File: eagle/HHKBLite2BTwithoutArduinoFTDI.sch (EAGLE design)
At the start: 47 parts, among them CON1 45045-1445, CON2 45045-0845, IC1 4514N, IC2 4512N, IC4 HT7750A

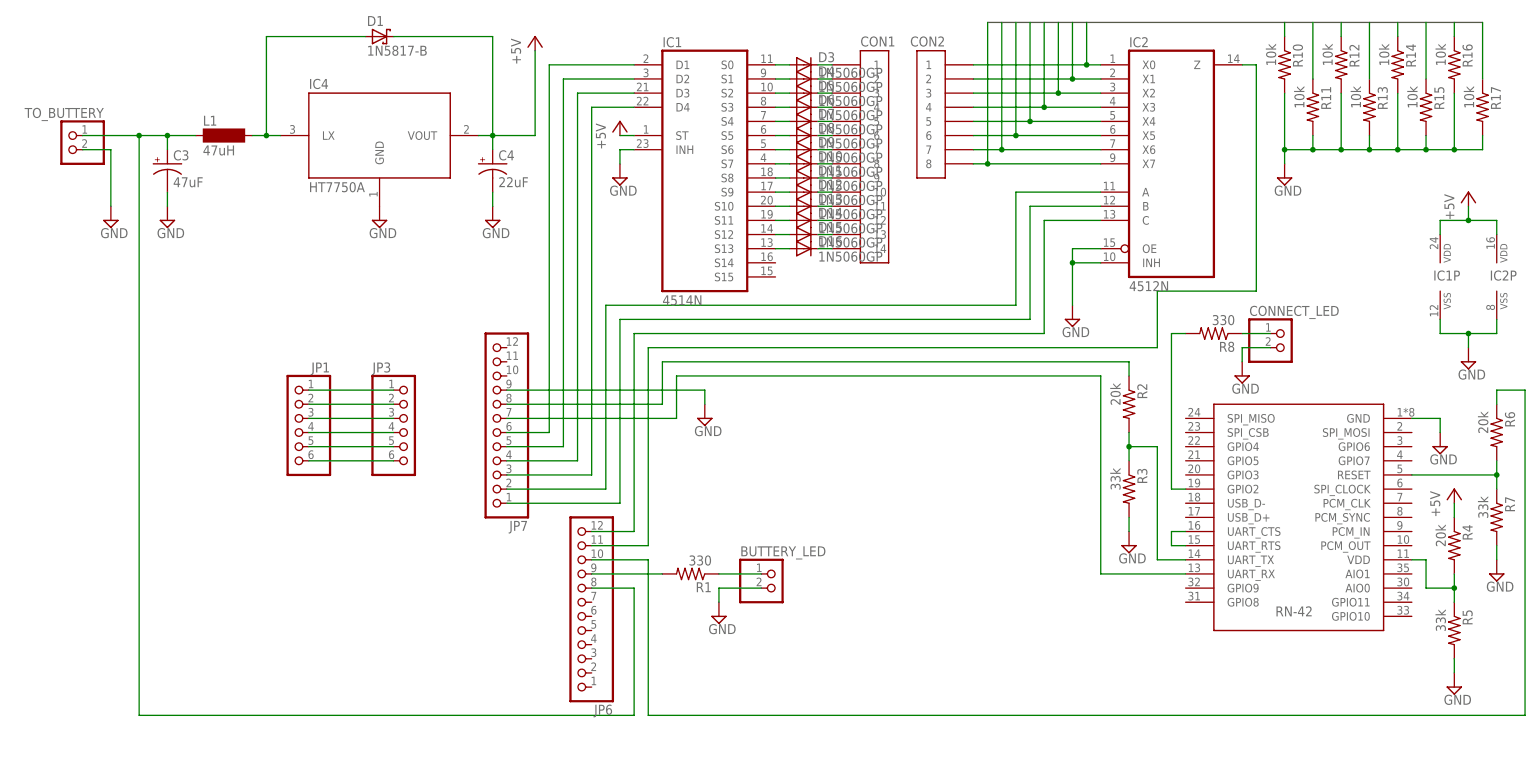
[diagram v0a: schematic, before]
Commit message: 基板を作成。
これまでは Arduino のpin1からpinNまでを順番につないでいたが、
基板に起こしやすいよう、接続の順番を基板用に書き換えた。
加えて、基板を作成した。
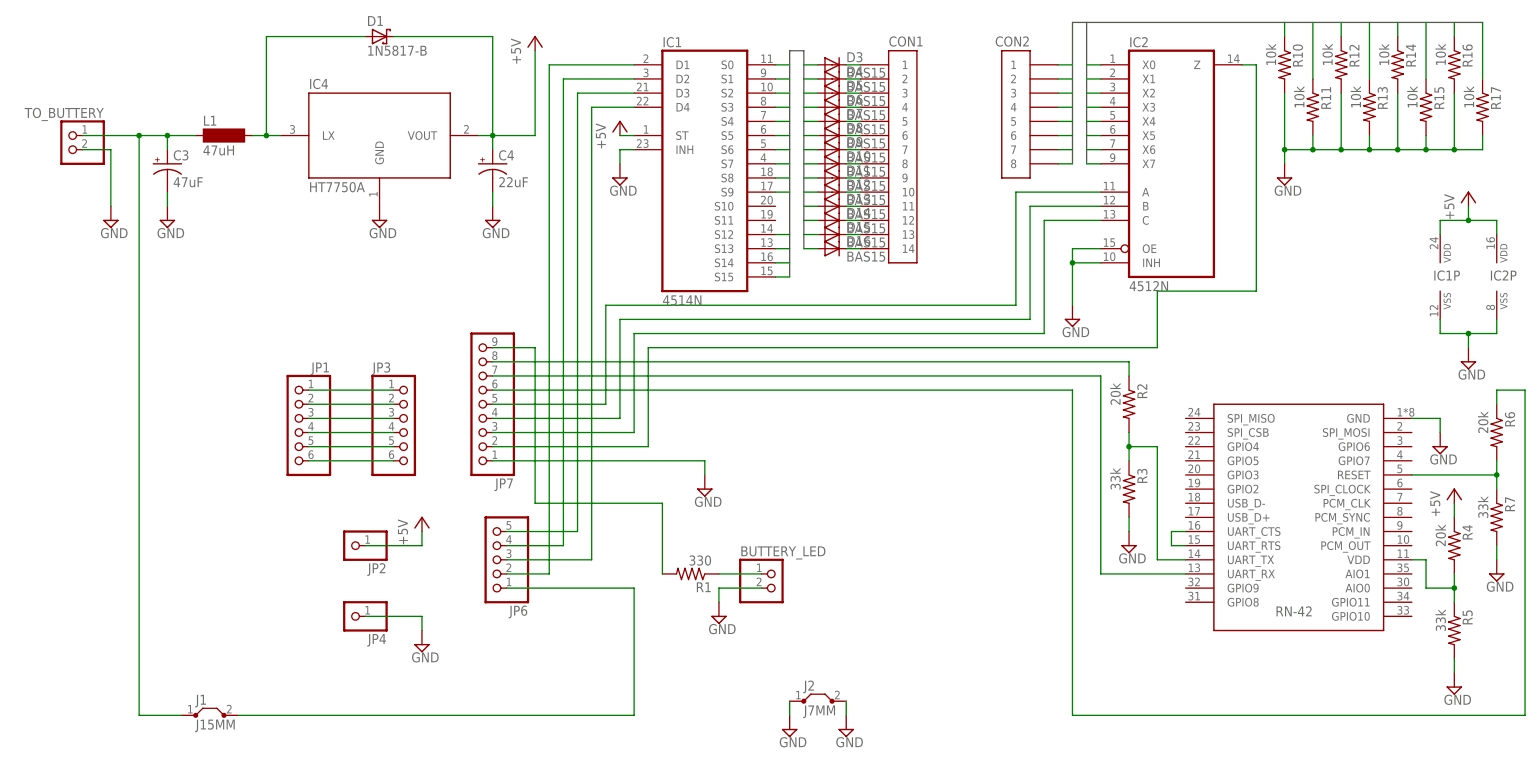
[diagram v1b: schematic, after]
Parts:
- removed CONNECT_LED: (no value), pinhead:PINHD-1X2
- removed R8: 330, rcl:R-US_0207/7
- added J1: J15MM, jumper:J15MM
- added J2: J7MM, jumper:J7MM
- added JP2, JP4: (no value), pinhead:PINHD-1X1
- D10, D11, D12, D13, D14, D15, D16, D3, D4, D5, D6, D7, D8, D9: value 1N5060GP -> BAS15; device diode:1N5060GP -> diode:BAS15
- JP6: device pinhead:PINHD-1X12 -> pinhead:PINHD-1X5
- JP7: device pinhead:PINHD-1X12 -> pinhead:PINHD-1X9
- R13: device rcl:R-US_0207/7 -> resistor:R-US_0207/10
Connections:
- net N$22 renamed CON1BUS_O0
- net N$25 renamed CON1BUS_O3
- net N$26 renamed CON1BUS_O4
- net N$27 renamed CON1BUS_O5
- net N$28 renamed CON1BUS_O6
- net N$29 renamed CON1BUS_O7
- net N$30 renamed CON1BUS_O8
- removed net CON2BUS1: CON2.1, IC2A.X0, R10.1
- removed net CON2BUS2: CON2.2, IC2A.X1, R11.1
- removed net CON2BUS3: CON2.3, IC2A.X2, R12.1
- removed net CON2BUS4: CON2.4, IC2A.X3, R13.1
- removed net CON2BUS5: CON2.5, IC2A.X4, R14.1
- removed net CON2BUS6: CON2.6, IC2A.X5, R15.1
- removed net CON2BUS7: CON2.7, IC2A.X6, R16.1
- removed net CON2BUS8: CON2.8, IC2A.X7, R17.1
- removed net N$15: IC2A.A, JP7.2
- removed net N$23: D4.A, IC1A.S1
- removed net N$24: D5.A, IC1A.S2
- removed net N$31: D12.A, IC1A.S9
- removed net N$32: D13.A, IC1A.S10
- removed net N$33: D14.A, IC1A.S11
- removed net N$34: D15.A, IC1A.S12
- removed net N$35: D16.A, IC1A.S13
- removed net N$40: R8.2, U$1.GPIO2
- removed net N$45: CONNECT_LED.1, R8.1
- new net CON1BUS_O1: D5.A, IC1A.S1
- new net CON1BUS_O12: D13.A, IC1A.S12
- new net CON1BUS_O13: D12.A, IC1A.S13
- new net CON1BUS_O14: D15.A, IC1A.S14
- new net CON1BUS_O15: D14.A, IC1A.S15
- new net CON1BUS_O2: D4.A, IC1A.S2
- new net CON1BUS_O9: D16.A, IC1A.S9
- new net CON2BUS_D0: CON2.8, IC2A.X0, R10.1
- new net CON2BUS_D1: CON2.7, IC2A.X1, R11.1
- new net CON2BUS_D2: CON2.6, IC2A.X2, R12.1
- new net CON2BUS_D3: CON2.5, IC2A.X3, R13.1
- new net CON2BUS_D4: CON2.4, IC2A.X4, R14.1
- new net CON2BUS_D5: CON2.3, IC2A.X5, R15.1
- new net CON2BUS_D6: CON2.2, IC2A.X6, R16.1
- new net CON2BUS_D7: CON2.1, IC2A.X7, R17.1
- new net N$14: JP7.9, R1.2
- new net N$22: IC2A.A, JP7.5
- net +5V: now also JP2.1
- net GND: now also J2.1, J2.2, JP4.1, JP7.1; no longer CONNECT_LED.2, JP7.9
- net N$12: now also J1.2, JP6.1; no longer JP6.9, R1.2
- net N$16: now also JP7.4; no longer JP7.1
- net N$17: now also JP7.3; no longer JP6.12
- net N$36: now also JP6.2; no longer JP7.6
- net N$37: now also JP6.4; no longer JP7.5
- net N$38: now also JP6.5; no longer JP7.4
- net N$39: now also JP6.3; no longer JP7.3
- net N$4: now also J1.1; no longer JP6.8
- net N$6: now also JP7.6; no longer JP6.10
- net N$9: now also JP7.2; no longer JP6.11
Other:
- moved on the sheet: CON1, CON2, D10, D11, D12, D13, D14, D15, D16, D3, D4, D5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
